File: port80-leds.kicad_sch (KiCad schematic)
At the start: 21 parts, among them U6001 SN74AC7541_VQFN, U6009 SN74AC7541_VQFN

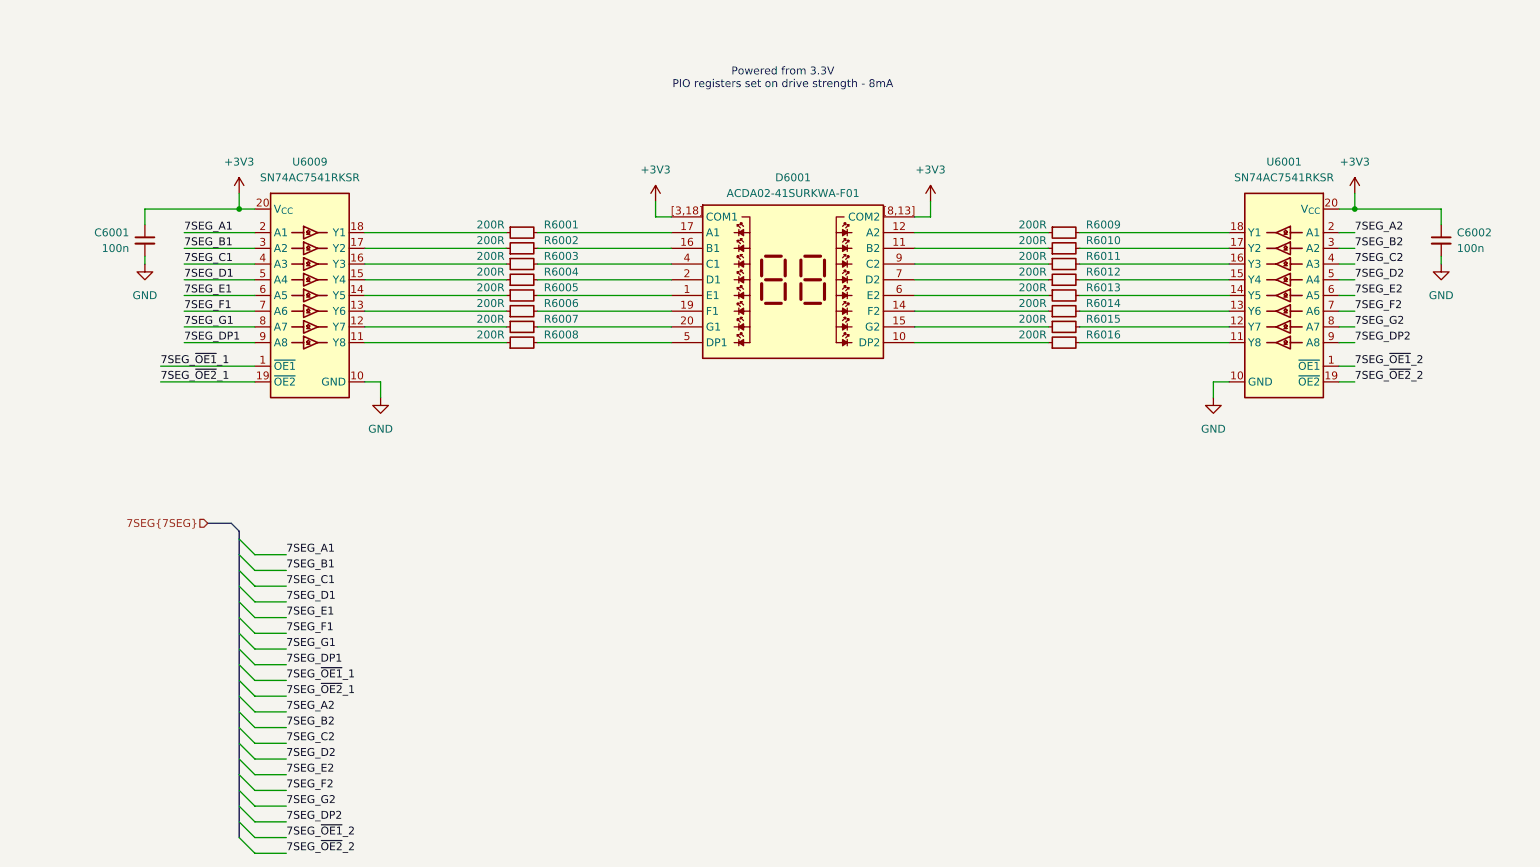
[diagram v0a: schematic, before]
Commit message: [#103224] Divide 7SEG bus into 2, rename JTAG connector pins
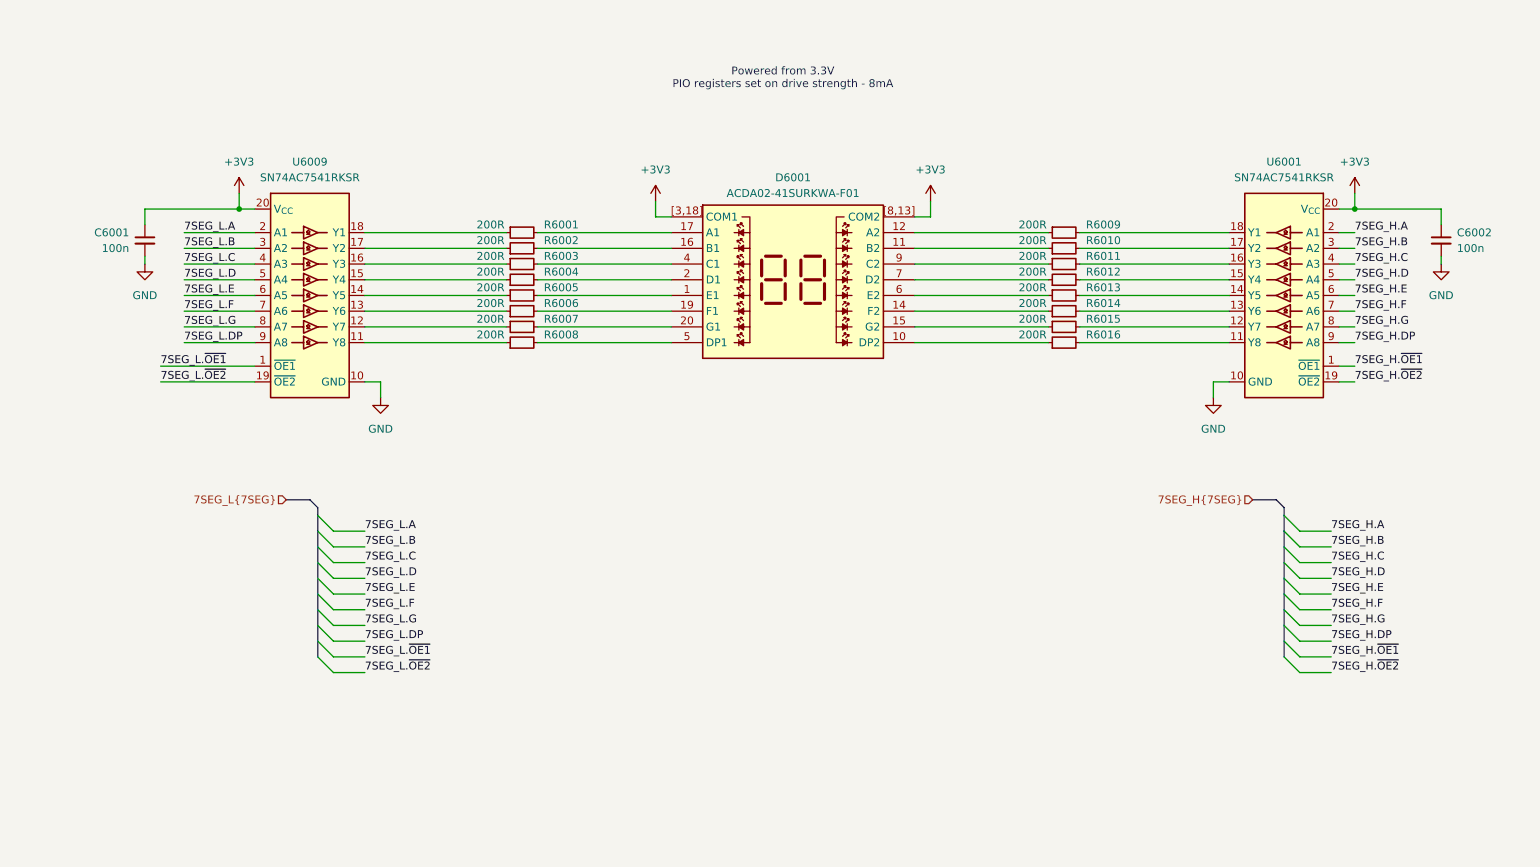
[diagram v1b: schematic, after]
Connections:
- net 7SEG_A1 renamed 7SEG_L.A
- net 7SEG_A2 renamed 7SEG_H.A
- net 7SEG_B1 renamed 7SEG_L.B
- net 7SEG_B2 renamed 7SEG_H.B
- net 7SEG_C1 renamed 7SEG_L.C
- net 7SEG_C2 renamed 7SEG_H.C
- net 7SEG_D1 renamed 7SEG_L.D
- net 7SEG_D2 renamed 7SEG_H.D
- net 7SEG_DP1 renamed 7SEG_L.DP
- net 7SEG_DP2 renamed 7SEG_H.DP
- net 7SEG_E1 renamed 7SEG_L.E
- net 7SEG_E2 renamed 7SEG_H.E
- net 7SEG_F1 renamed 7SEG_L.F
- net 7SEG_F2 renamed 7SEG_H.F
- net 7SEG_G1 renamed 7SEG_L.G
- net 7SEG_G2 renamed 7SEG_H.G
- net 7SEG_~{OE1}_1 renamed 7SEG_L.~{OE1}
- net 7SEG_~{OE1}_2 renamed 7SEG_H.~{OE1}
- net 7SEG_~{OE2}_1 renamed 7SEG_L.~{OE2}
- net 7SEG_~{OE2}_2 renamed 7SEG_H.~{OE2}

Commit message: [#103224] Add UART1, added GND to breakout connectors, fix orientation of DC-SCM connector, delete unused notes
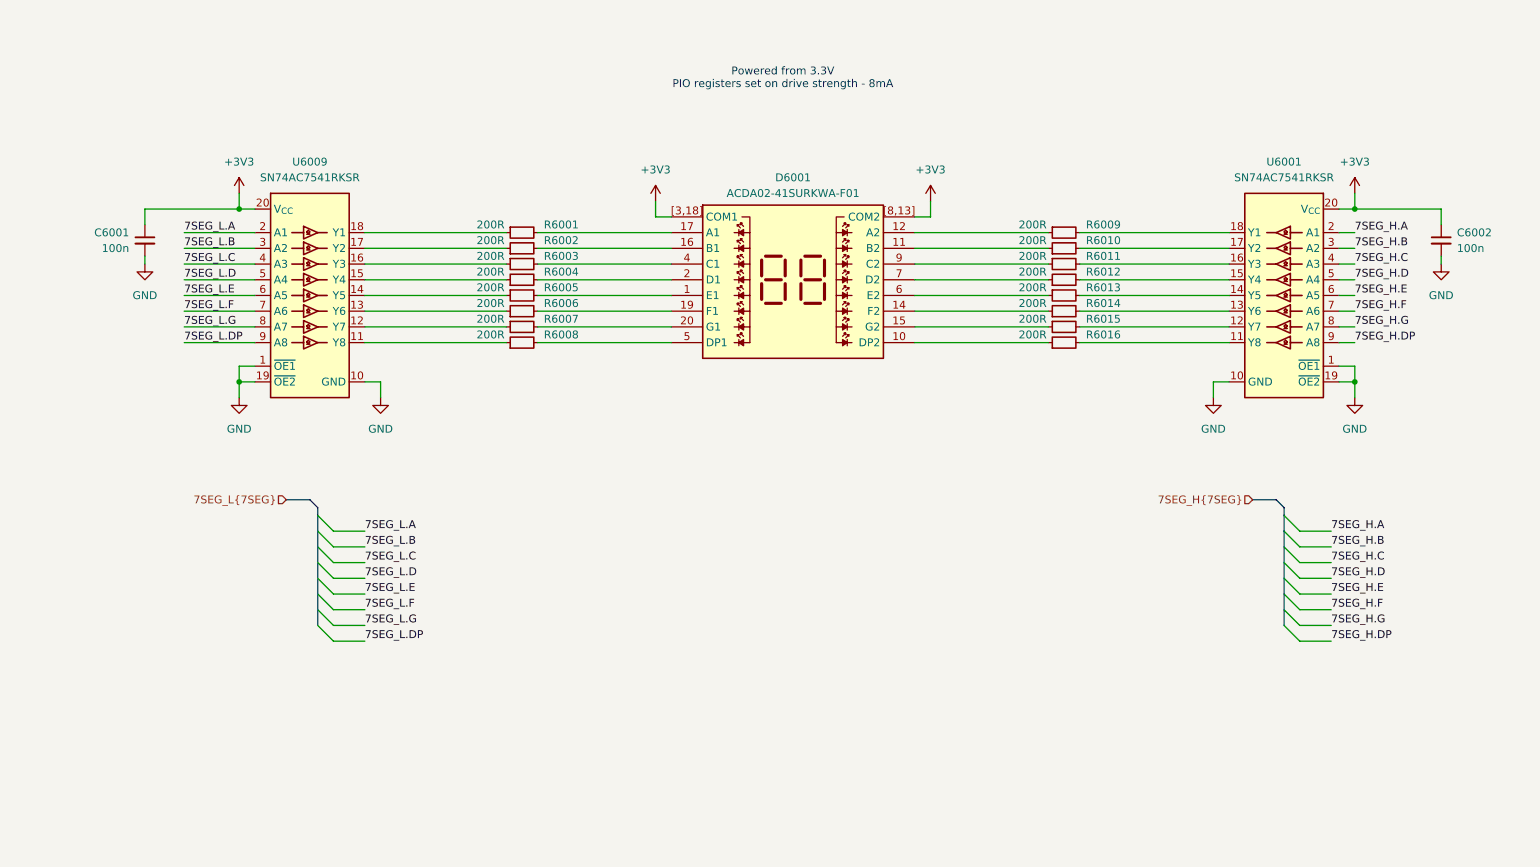
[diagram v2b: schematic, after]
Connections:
- net 7SEG_H.~{OE1} is gone; now on net GND: U6001.1 (~{OE1})
- net 7SEG_H.~{OE2} is gone; now on net GND: U6001.19 (~{OE2})
- net 7SEG_L.~{OE1} is gone; now on net GND: U6009.1 (~{OE1})
- net 7SEG_L.~{OE2} is gone; now on net GND: U6009.19 (~{OE2})

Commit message: chore: set date and project name
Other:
- company: (none) -> Antmicro
- title: (none) -> eSPI Adapter
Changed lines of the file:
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@@
 	(generator_version "10.0")
 	(paper "A4")
+	(title_block
+		(title "eSPI Adapter")
+		(date "2026-08-21")
+		(rev "1.0.0")
+		(company "Antmicro")
+	)
 	(text "Powered from 3.3V\nPIO registers set on drive strength - 8mA"
 		(exclude_from_sim no)

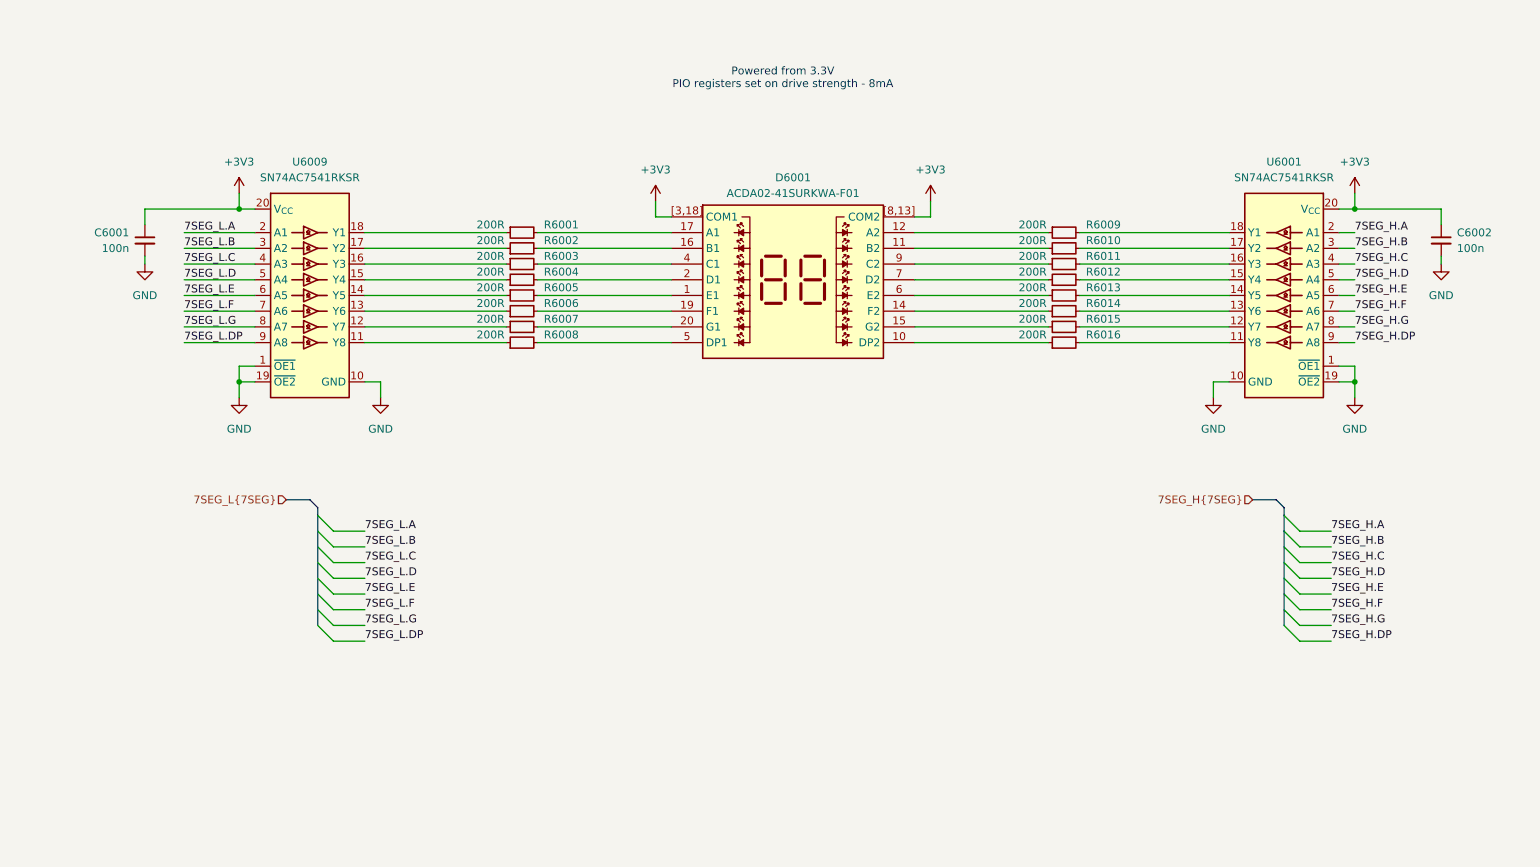
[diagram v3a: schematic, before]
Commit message: [#103224] port80-leds: swap H/L, add missing signal labels
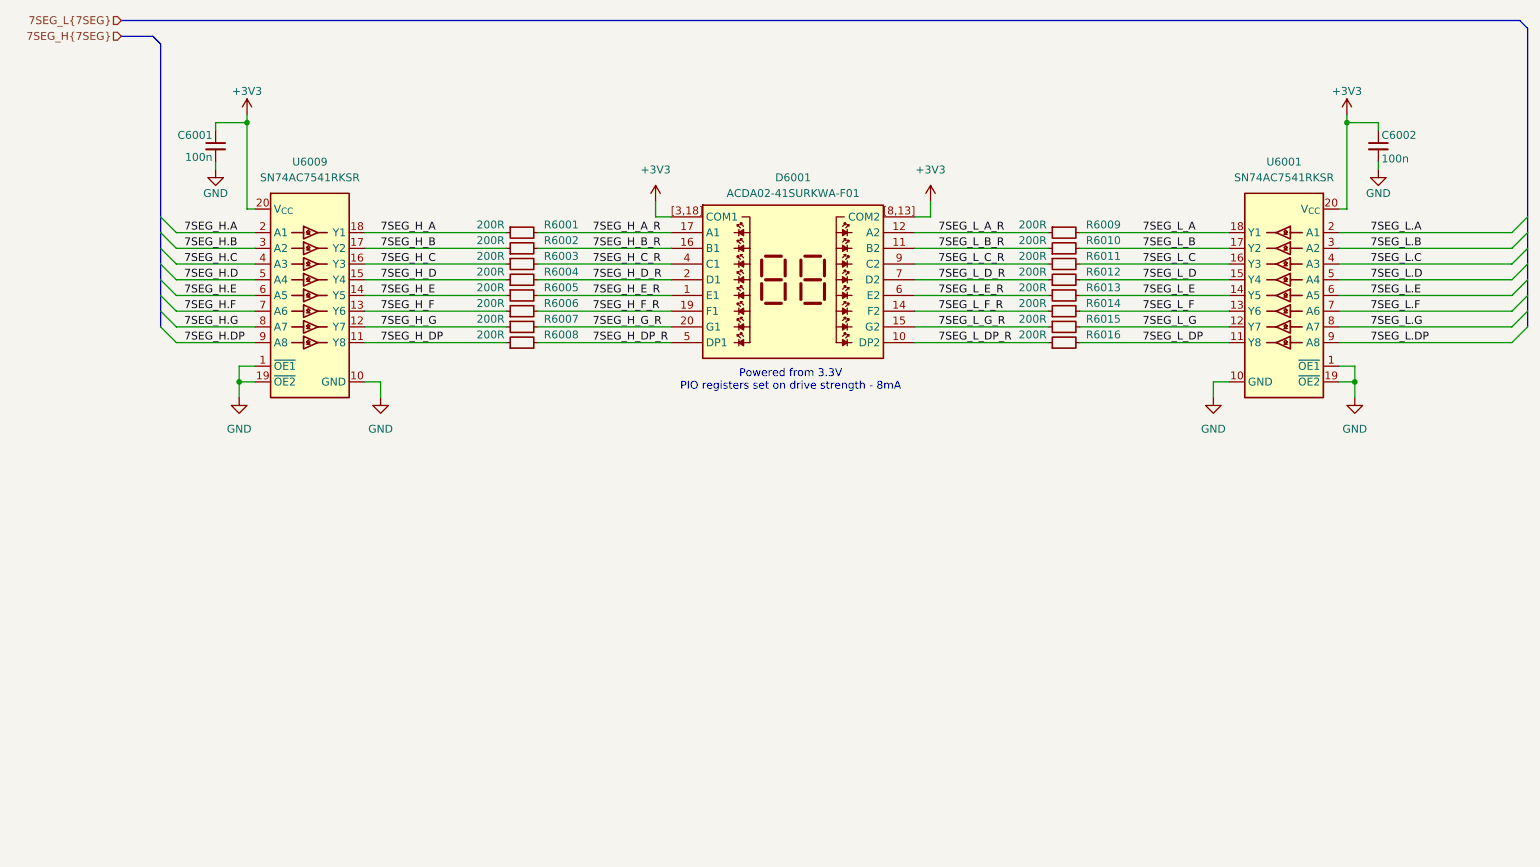
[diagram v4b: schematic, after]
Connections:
- net 7SEG_H.A: now also U6009.2 (A1); no longer U6001.2 (A1)
- net 7SEG_H.B: now also U6009.3 (A2); no longer U6001.3 (A2)
- net 7SEG_H.C: now also U6009.4 (A3); no longer U6001.4 (A3)
- net 7SEG_H.D: now also U6009.5 (A4); no longer U6001.5 (A4)
- net 7SEG_H.DP: now also U6009.9 (A8); no longer U6001.9 (A8)
- net 7SEG_H.E: now also U6009.6 (A5); no longer U6001.6 (A5)
- net 7SEG_H.F: now also U6009.7 (A6); no longer U6001.7 (A6)
- net 7SEG_H.G: now also U6009.8 (A7); no longer U6001.8 (A7)
- net 7SEG_L.A: now also U6001.2 (A1); no longer U6009.2 (A1)
- net 7SEG_L.B: now also U6001.3 (A2); no longer U6009.3 (A2)
- net 7SEG_L.C: now also U6001.4 (A3); no longer U6009.4 (A3)
- net 7SEG_L.D: now also U6001.5 (A4); no longer U6009.5 (A4)
- net 7SEG_L.DP: now also U6001.9 (A8); no longer U6009.9 (A8)
- net 7SEG_L.E: now also U6001.6 (A5); no longer U6009.6 (A5)
- net 7SEG_L.F: now also U6001.7 (A6); no longer U6009.7 (A6)
- net 7SEG_L.G: now also U6001.8 (A7); no longer U6009.8 (A7)
- net 7SEG_H_E_R: now reaches D6001.1 (E1), R6005.2
- net 7SEG_L_DP_R: now reaches D6001.10 (DP2), R6016.1
- net 7SEG_L_B_R: now reaches D6001.11 (B2), R6010.1
- net 7SEG_L_A_R: now reaches D6001.12 (A2), R6009.1
- net 7SEG_L_F_R: now reaches D6001.14 (F2), R6014.1
- net 7SEG_L_G_R: now reaches D6001.15 (G2), R6015.1
- net 7SEG_H_B_R: now reaches D6001.16 (B1), R6002.2
- net 7SEG_H_A_R: now reaches D6001.17 (A1), R6001.2
- net 7SEG_H_F_R: now reaches D6001.19 (F1), R6006.2
- net 7SEG_H_D_R: now reaches D6001.2 (D1), R6004.2
- net 7SEG_H_G_R: now reaches D6001.20 (G1), R6007.2
- net 7SEG_H_C_R: now reaches D6001.4 (C1), R6003.2
- net 7SEG_H_DP_R: now reaches D6001.5 (DP1), R6008.2
- net 7SEG_L_E_R: now reaches D6001.6 (E2), R6013.1
- net 7SEG_L_D_R: now reaches D6001.7 (D2), R6012.1
- net 7SEG_L_C_R: now reaches D6001.9 (C2), R6011.1
- net 7SEG_L_DP: now reaches R6016.2, U6001.11 (Y8)
- net 7SEG_L_G: now reaches R6015.2, U6001.12 (Y7)
- net 7SEG_L_F: now reaches R6014.2, U6001.13 (Y6)
- net 7SEG_L_E: now reaches R6013.2, U6001.14 (Y5)
- net 7SEG_L_D: now reaches R6012.2, U6001.15 (Y4)
- net 7SEG_L_C: now reaches R6011.2, U6001.16 (Y3)
- net 7SEG_L_B: now reaches R6010.2, U6001.17 (Y2)
- net 7SEG_L_A: now reaches R6009.2, U6001.18 (Y1)
- net 7SEG_H_E: now reaches R6005.1, U6009.14 (Y5)
- net 7SEG_H_D: now reaches R6004.1, U6009.15 (Y4)
- net 7SEG_H_DP: now reaches R6008.1, U6009.11 (Y8)
- net 7SEG_H_G: now reaches R6007.1, U6009.12 (Y7)
- net 7SEG_H_F: now reaches R6006.1, U6009.13 (Y6)
- net 7SEG_H_C: now reaches R6003.1, U6009.16 (Y3)
- net 7SEG_H_B: now reaches R6002.1, U6009.17 (Y2)
- net 7SEG_H_A: now reaches R6001.1, U6009.18 (Y1)
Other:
- moved on the sheet: C6001, C6002

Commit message: [#103753] Fix issues according to the review, add FT2232 to the schematic
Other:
- note removed: "Powered from 3.3V PIO registers set on drive strength - 8mA"
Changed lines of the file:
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@@
 		(company "Antmicro")
-	)
-	(text "Powered from 3.3V\nPIO registers set on drive strength - 8mA"
-		(exclude_from_sim no)
-		(at 143.764 106.426 0)
-		(effects
-			(font
-				(size 1.27 1.27)
-			)
-		)
 	)
 	(junction

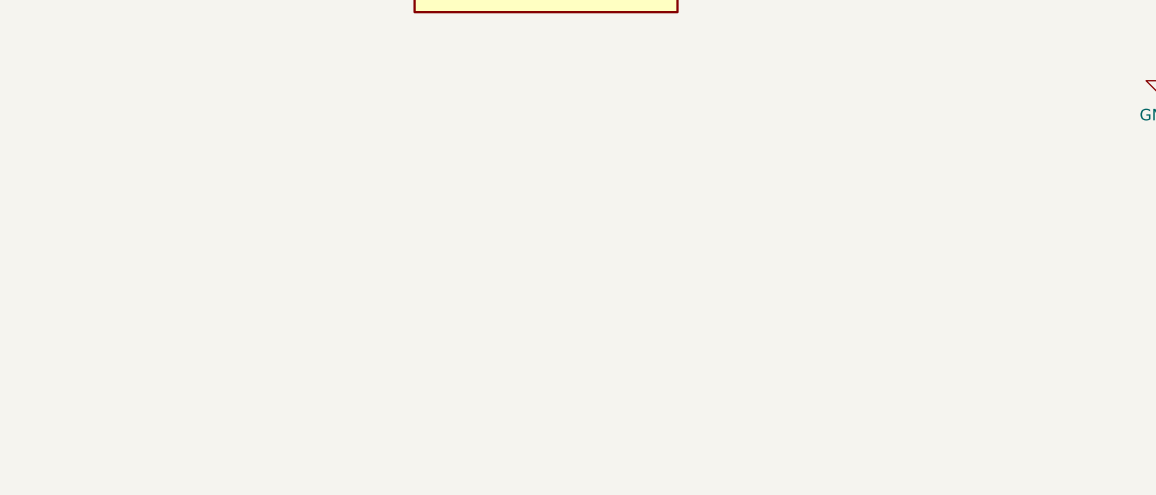
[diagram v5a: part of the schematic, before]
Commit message: [#103753] Fix issues according to the review, add redundant LEDs, delete fp-lib-table
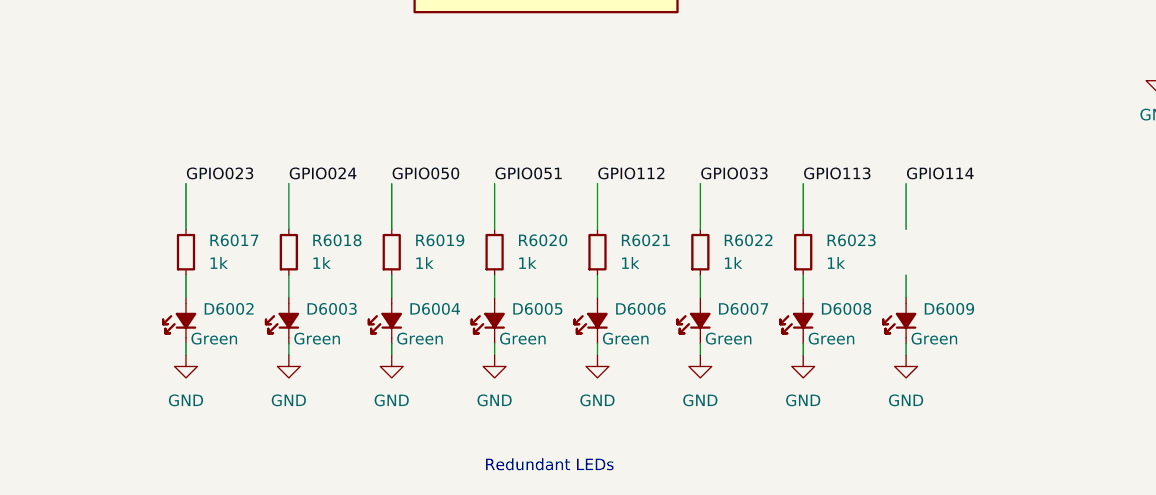
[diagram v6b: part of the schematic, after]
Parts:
- added D6002, D6003, D6004, D6005, D6006, D6007, D6008, D6009: LED_G_0603_LTST-C190GKT, antmicro-footprints:LED_0603_1608Metric_G, symbol antmicroLEDIndicationDiscrete:LED_G_0603_LTST-C190GKT
- added R6017, R6018, R6019, R6020, R6021, R6022, R6023: R_1k_0402, antmicro-footprints:R_0402_1005Metric, symbol Antmicro Symbols:R_1k_0402
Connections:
- net GND: now also D6002.1 (C), D6003.1 (C), D6004.1 (C), D6005.1 (C), D6006.1 (C), D6007.1 (C), D6008.1 (C), D6009.1 (C)
- new net: D6007.2 (A), R6022.1
- new net: D6002.2 (A), R6017.1
- new net: D6004.2 (A), R6019.1
- new net: D6006.2 (A), R6021.1
- new net: D6005.2 (A), R6020.1
- new net: D6003.2 (A), R6018.1
- new net: D6008.2 (A), R6023.1
- new net GPIO023: R6017.2
- new net GPIO024: R6018.2
- new net GPIO033: R6022.2
- new net GPIO050: R6019.2
- new net GPIO051: R6020.2
- new net GPIO112: R6021.2
- new net GPIO113: R6023.2
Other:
- note added: "Redundant LEDs"
